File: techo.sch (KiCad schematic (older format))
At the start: 14 parts

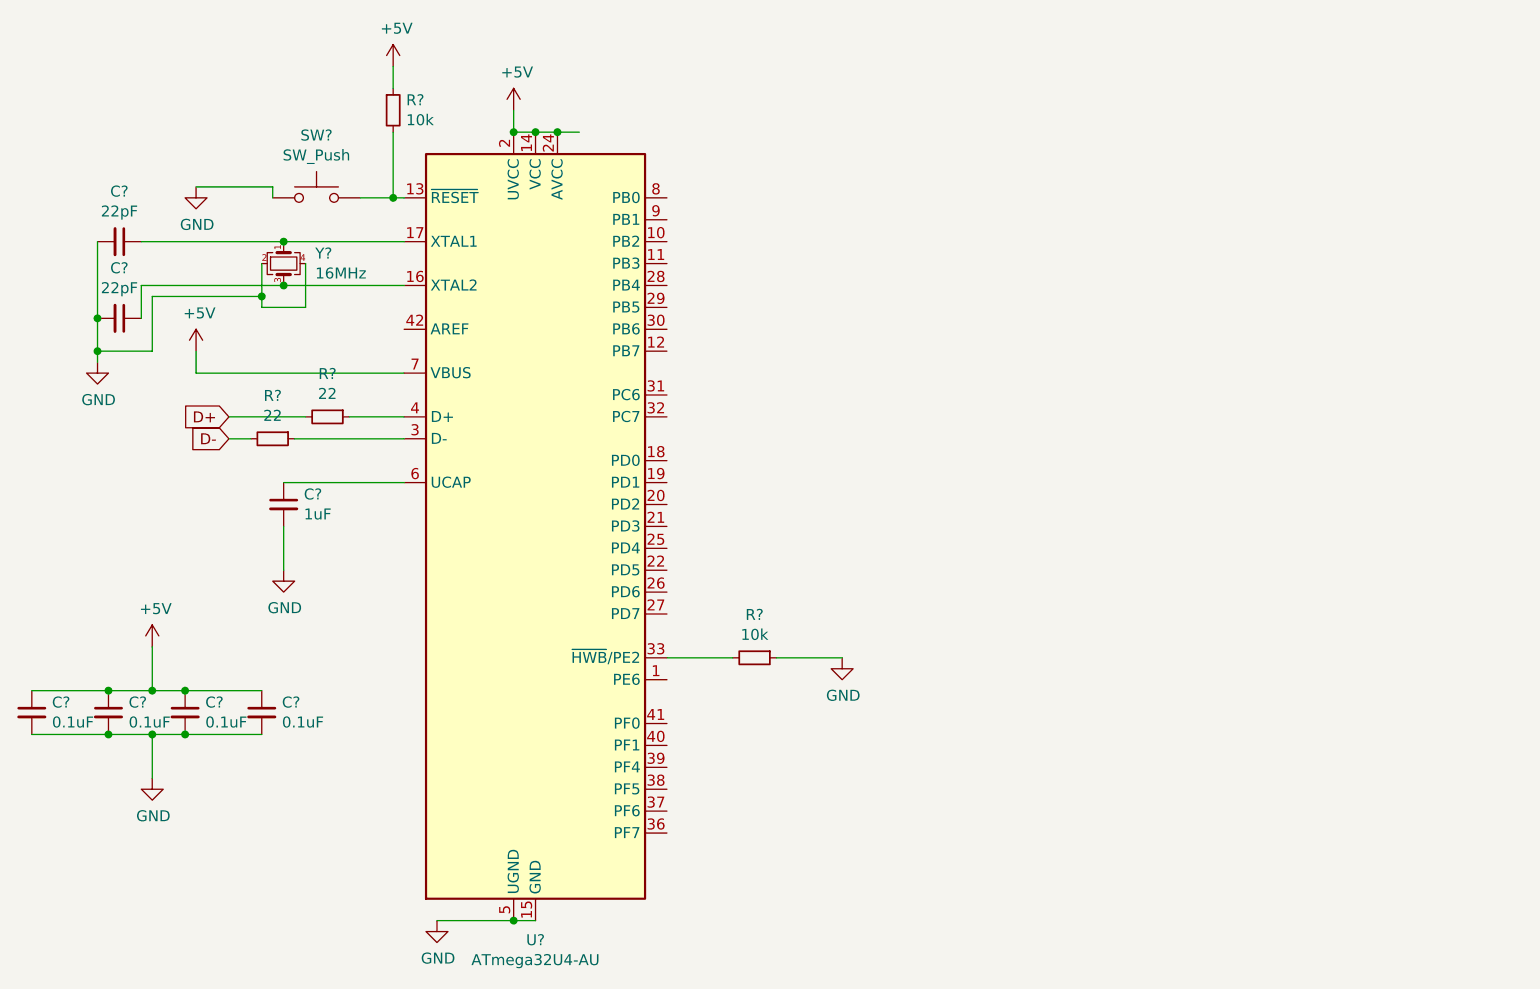
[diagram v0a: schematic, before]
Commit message: Schematic done
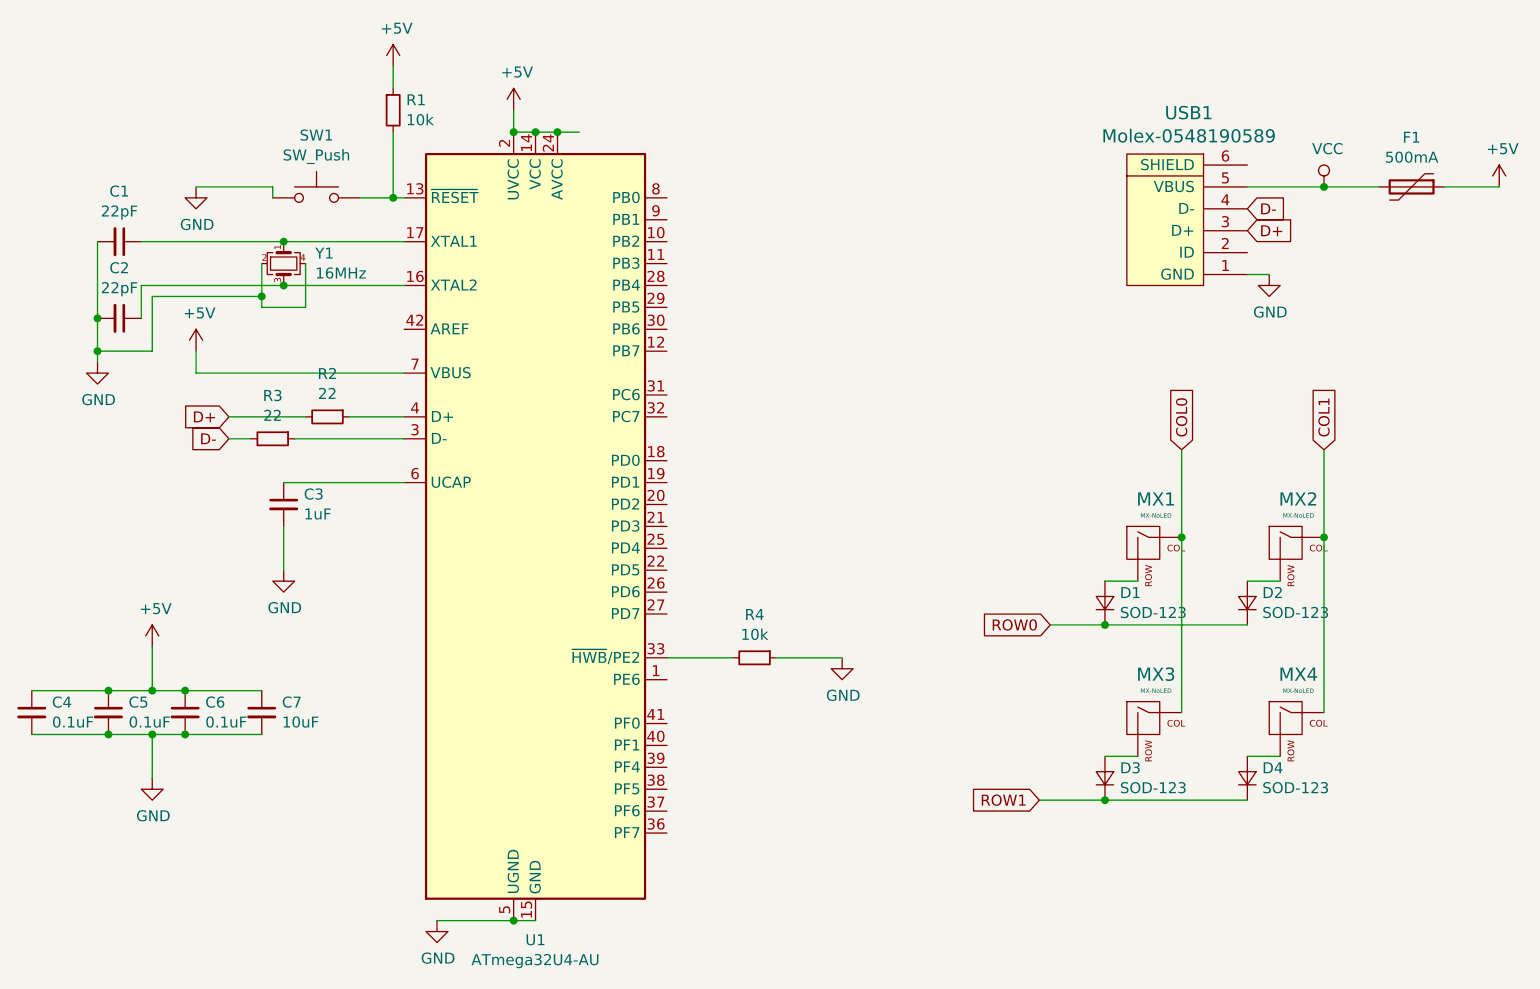
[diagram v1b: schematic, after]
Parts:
- added D1, D2, D3, D4: SOD-123, Diode_SMD:D_SOD-123, symbol Device:D_Small
- added F1: 500mA, Fuse:Fuse_1206_3216Metric, symbol Device:Polyfuse
- added MX1, MX2, MX3, MX4: MX-NoLED, MX_Alps_Hybrid:MX-1U, symbol MX_Alps_Hybrid:MX-NoLED
- added USB1: Molex-0548190589, random-keyboard-parts:Molex-0548190589, symbol random-keyboard-parts:Molex-0548190589
- C1, C2, C3, C4, C5, C6: renamed from C?; footprint (none) -> Capacitor_SMD:C_0805_2012Metric
- C7: renamed from C?; value 0.1uF -> 10uF; footprint (none) -> Capacitor_SMD:C_0805_2012Metric
- R1, R2, R3, R4: renamed from R?; footprint (none) -> Resistor_SMD:R_0805_2012Metric
- SW1: renamed from SW?; footprint (none) -> random-keyboard-parts:SKQG-1155865
- Y1: renamed from Y?; footprint (none) -> Crystal:Crystal_SMD_3225-4Pin_3.2x2.5mm
- gave numbers to parts that had none: 1
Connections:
- net +5V: now also F1.1
- net D+: now also USB1.3 (D+)
- net D-: now also USB1.4 (D-)
- net GND: now also USB1.1 (GND)
- new net: D1.2 (A), MX1.2 (ROW)
- new net: D2.2 (A), MX2.2 (ROW)
- new net: D3.2 (A), MX3.2 (ROW)
- new net: D4.2 (A), MX4.2 (ROW)
- new net COL0: MX1.1 (COL), MX3.1 (COL)
- new net COL1: MX2.1 (COL), MX4.1 (COL)
- new net ROW0: D1.1 (K), D2.1 (K)
- new net ROW1: D3.1 (K), D4.1 (K)
- new net VCC: F1.2, USB1.5 (VBUS)

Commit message: Completed tutorial
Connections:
- net COL0: now also U1.29 (PB5)
- net COL1: now also U1.28 (PB4)
- net ROW0: now also U1.27 (PD7)
- net ROW1: now also U1.30 (PB6)
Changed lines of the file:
@@
 Text GLabel 5200 4250 0    50   Input ~ 0
 ROW1
+Text GLabel 3500 1900 2    50   Input ~ 0
+COL1
+Text GLabel 3500 2000 2    50   Input ~ 0
+COL0
+Text GLabel 3500 2100 2    50   Input ~ 0
+ROW1
+Text GLabel 3500 3400 2    50   Input ~ 0
+ROW0
 $EndSCHEMATC

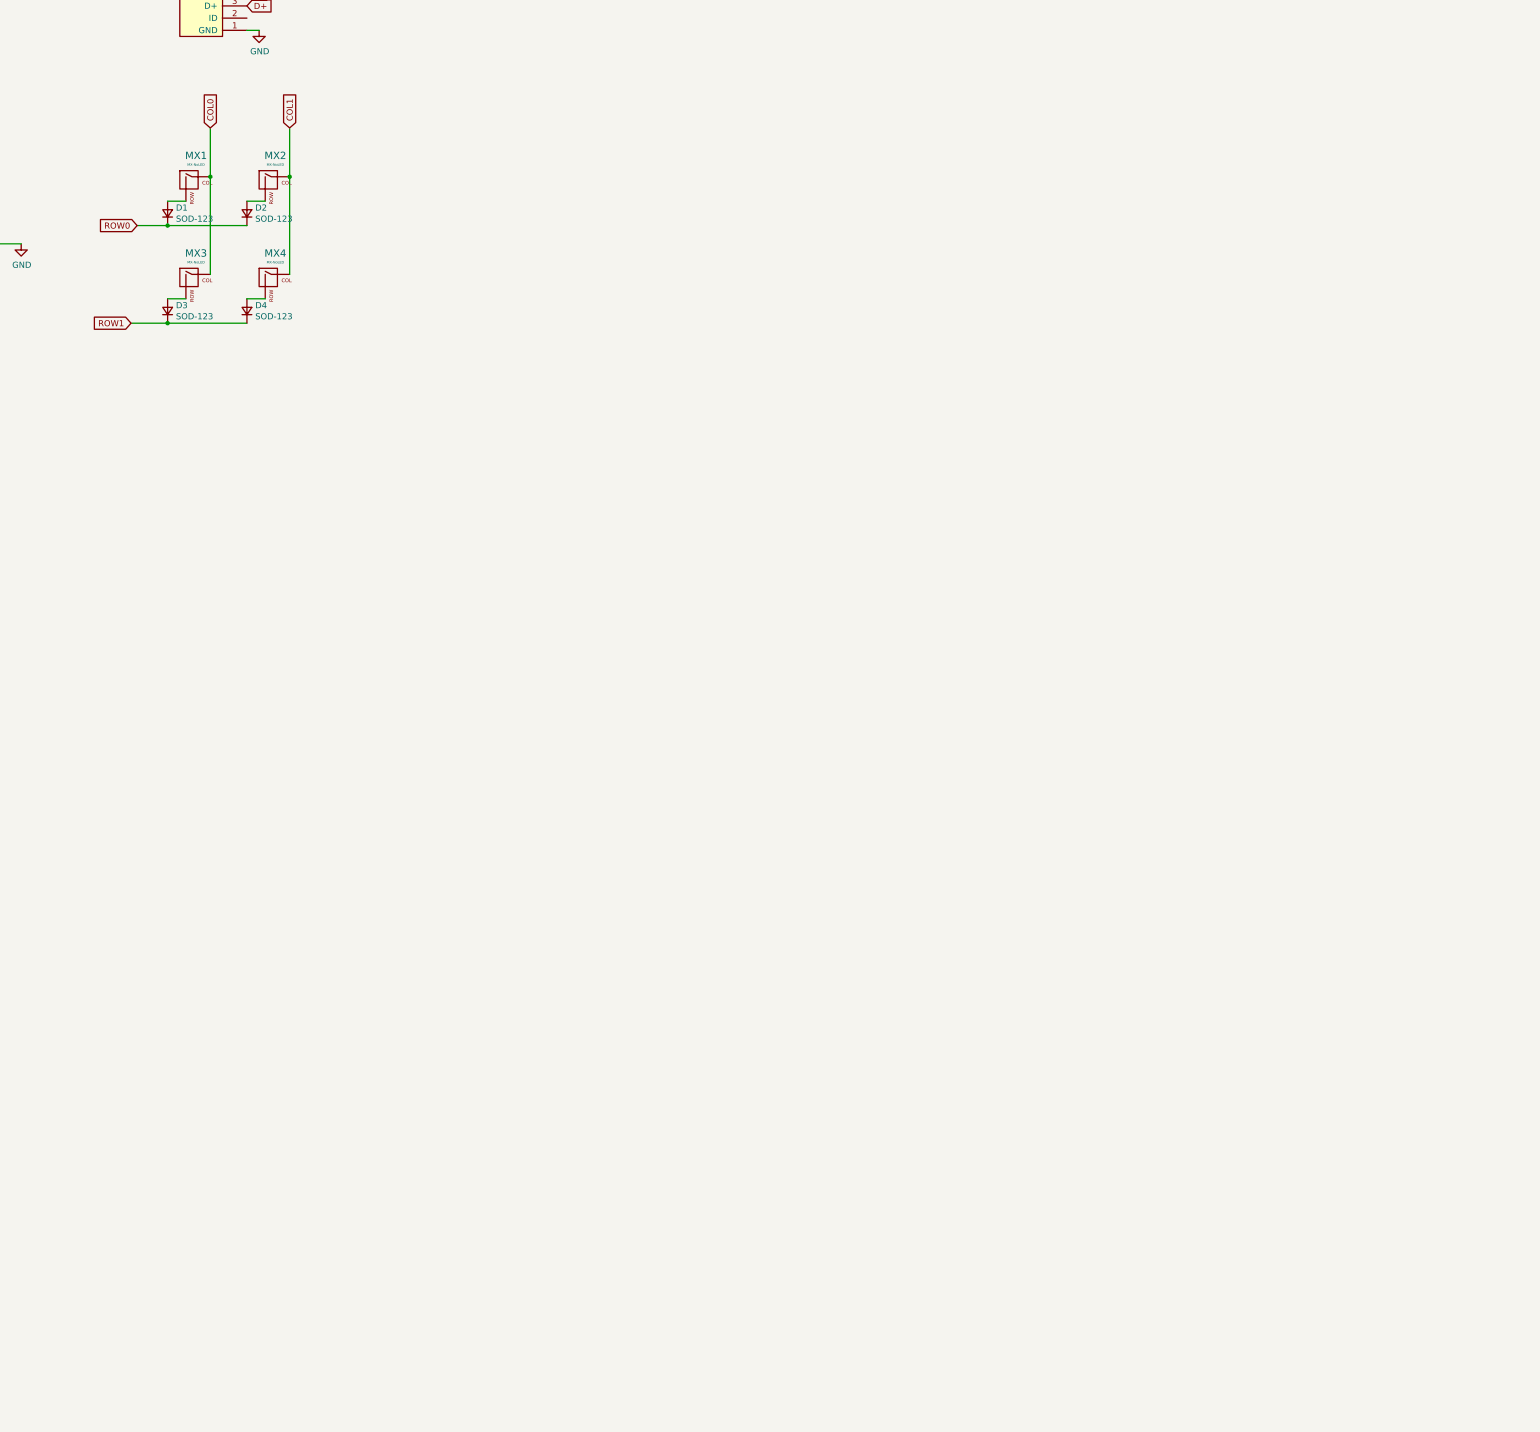
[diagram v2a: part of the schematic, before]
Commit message: Started making keyboard matrix
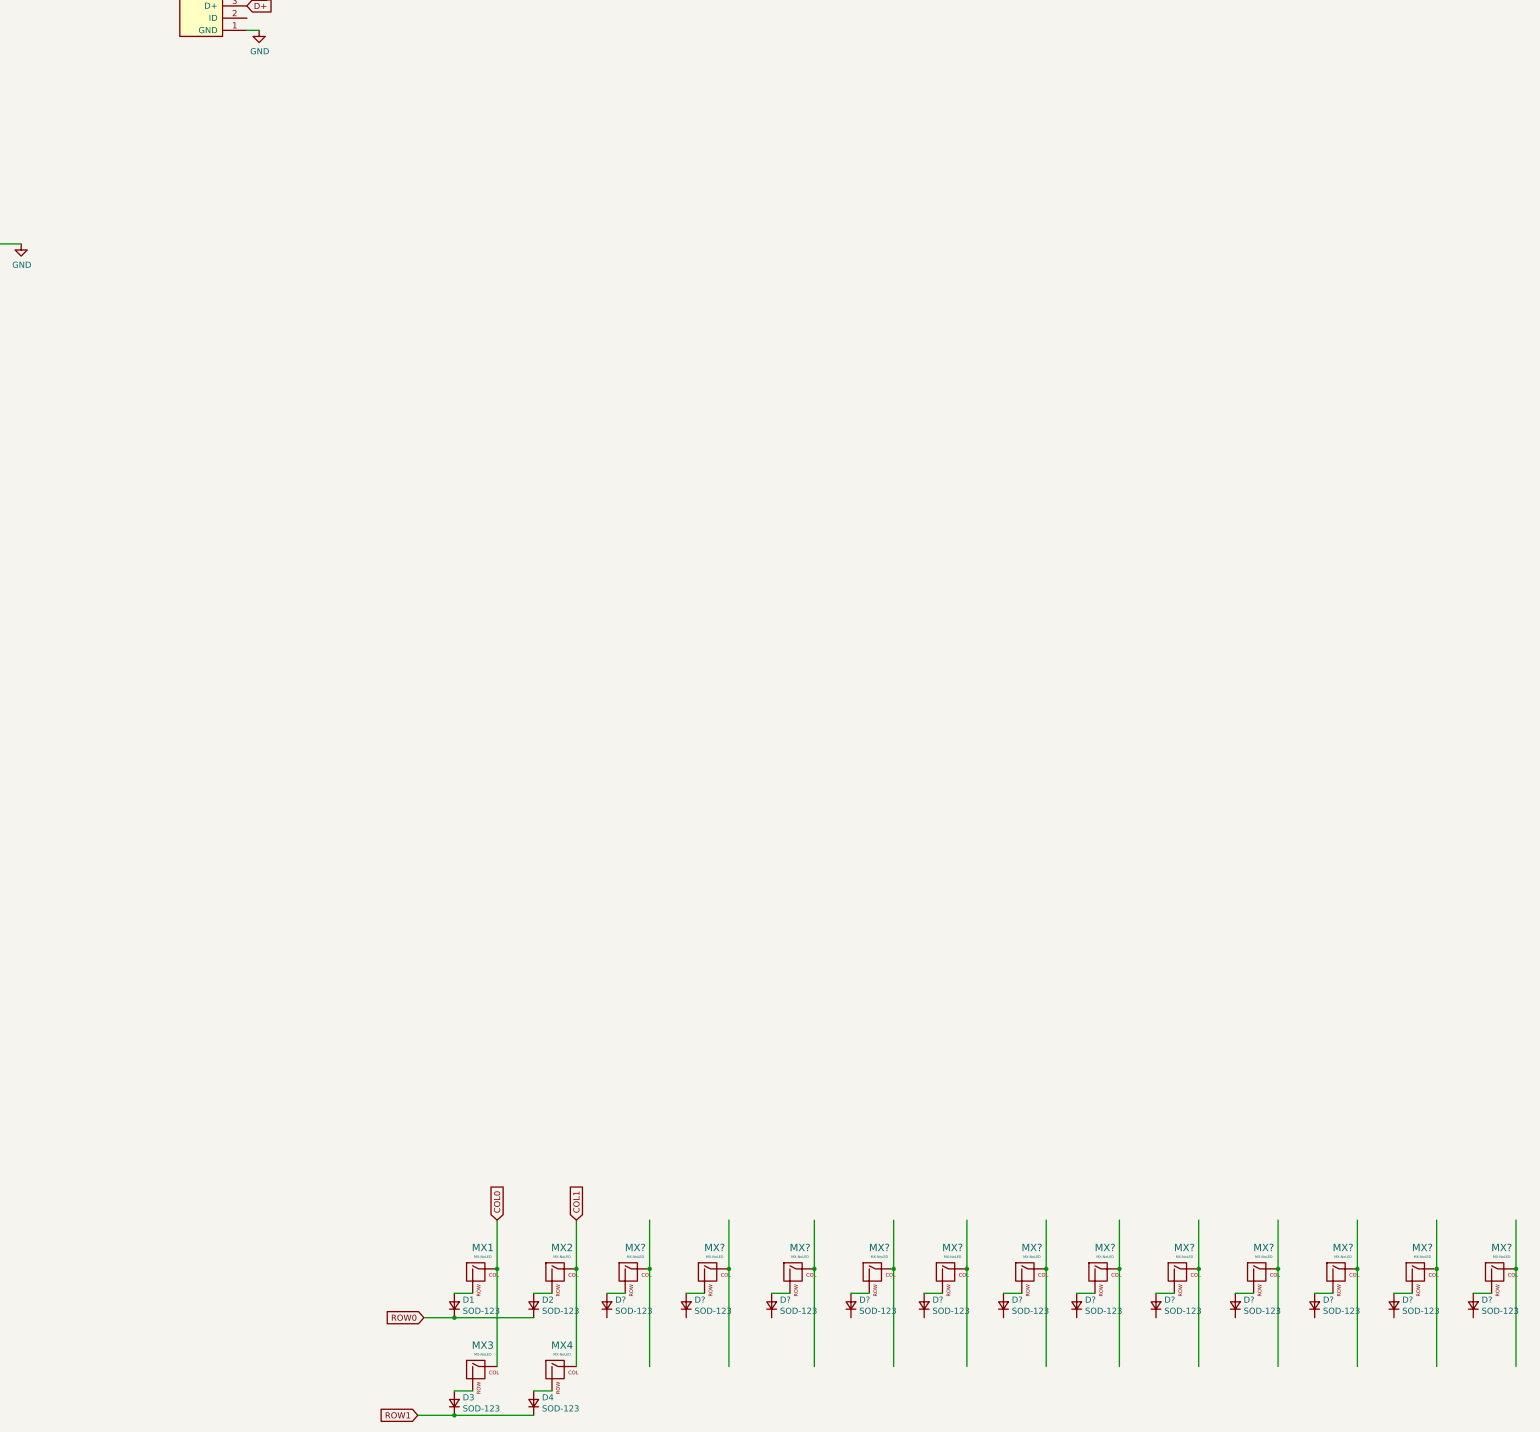
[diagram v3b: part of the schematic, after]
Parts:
- added D? (x12): SOD-123, Diode_SMD:D_SOD-123, symbol Device:D_Small
- added MX? (x12): MX-NoLED, MX_Alps_Hybrid:MX-1U, symbol MX_Alps_Hybrid:MX-NoLED
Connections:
- wire segments 63 -> 99
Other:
- moved on the sheet: D1, D2, D3, D4, MX1, MX2, MX3, MX4

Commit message: Researching usage of ATmega32A
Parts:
- added D10, D11, D12, D13, D15, D16, D17, D18, D19, D21, D22, D23, D24, D25, D27, D28, D29, D30, D31, D33, D34, D35, D36, D37, D39, D40, D41, D42, D43, D45, D46, D47, D48, D49, D5, D51, D52, D53, D54, D55, D57, D58, D59, D6, D60, D61, D63, D64, D65, D66, D67, D69, D7, D70, D71, D72, D74, D75, D76, D77, D79, D8, D80, D81, D82, D83, D84, D85, D86, D87, D88, D9: SOD-123, Diode_SMD:D_SOD-123, symbol Device:D_Small
- added MX10, MX11, MX12, MX13, MX15, MX16, MX17, MX18, MX19, MX21, MX22, MX23, MX24, MX25, MX27, MX28, MX29, MX30, MX31, MX33, MX34, MX35, MX36, MX37, MX39, MX40, MX41, MX42, MX43, MX45, MX46, MX47, MX48, MX49, MX5, MX51, MX52, MX53, MX54, MX55, MX57, MX58, MX59, MX6, MX60, MX61, MX63, MX64, MX65, MX66, MX67, MX69, MX7, MX70, MX71, MX72, MX74, MX75, MX76, MX77, MX79, MX8, MX80, MX81, MX82, MX83, MX84, MX85, MX86, MX87, MX88, MX9: MX-NoLED, MX_Alps_Hybrid:MX-1U, symbol MX_Alps_Hybrid:MX-NoLED
- added U?: ATmega32A-PU, Package_DIP:DIP-40_W15.24mm, symbol MCU_Microchip_ATmega:ATmega32A-PU
- gave numbers to parts that had none: 24
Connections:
- net labels added: COL10, COL11, COL12, COL13, COL14, COL15, COL16, COL2, COL3, COL4, COL5, COL6, COL7, COL8, COL9, ROW2, ROW3, ROW4, ROW5
- wire segments 99 -> 363
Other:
- moved on the sheet: C1, C2, D1, D14, D2, D20, D26, D32, D38, D44, D50, D56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

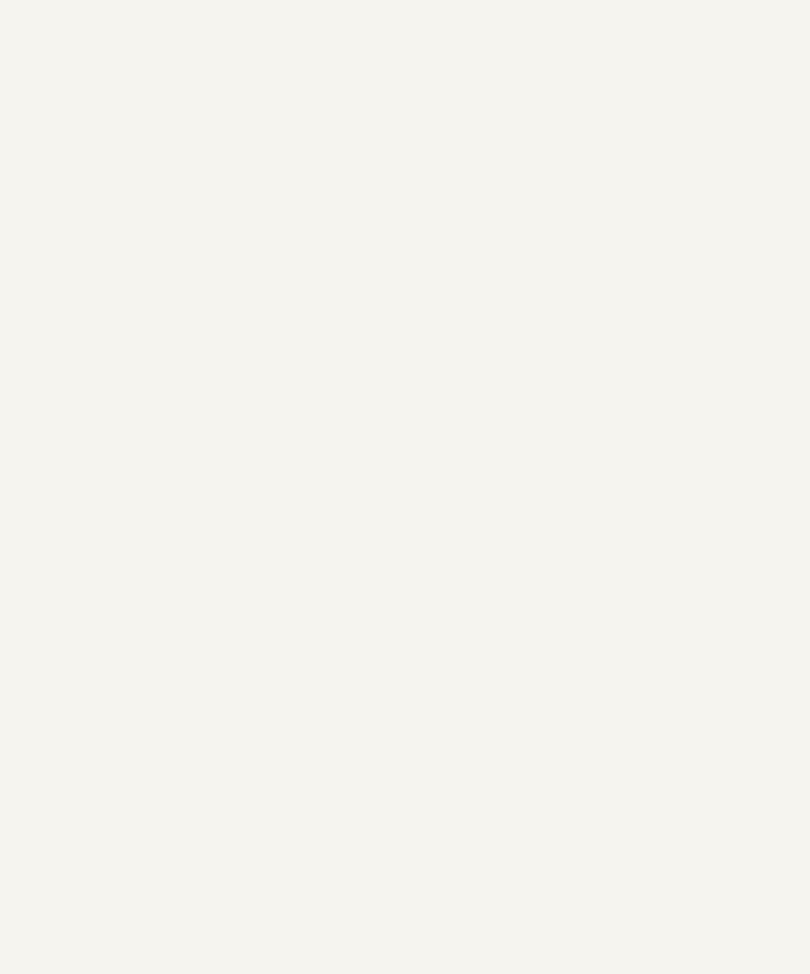
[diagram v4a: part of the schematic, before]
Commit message: Added Raspberry pi pinout
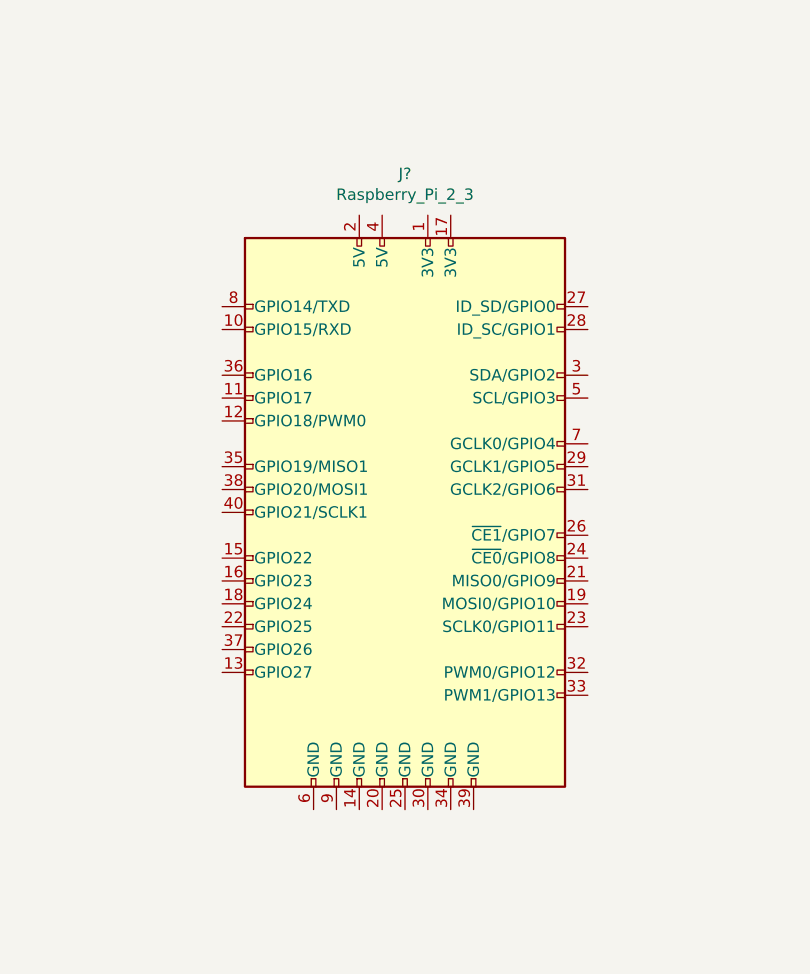
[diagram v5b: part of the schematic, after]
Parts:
- added J?: Raspberry_Pi_2_3, symbol Connector:Raspberry_Pi_2_3
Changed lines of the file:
@@
 Connection ~ 5250 1850
 Connection ~ 4850 1850
+$Comp
+L Connector:Raspberry_Pi_2_3 J?
+U 1 1 60969EEE
+P 8850 3950
+F 0 "J?" H 8850 5431 50  0000 C CNN
+F 1 "Raspberry_Pi_2_3" H 8850 5340 50  0000 C CNN
+F 2 "" H 8850 3950 50  0001 C CNN
+F 3 "https://www.raspberrypi.org/documentation/hardware/raspberrypi/schematics/rpi_SCH_3bplus_1p0_reduced.pdf" H 8850 3950 50  0001 C CNN
+	1    8850 3950
+	1    0    0    -1
+$EndComp
 $EndSCHEMATC
